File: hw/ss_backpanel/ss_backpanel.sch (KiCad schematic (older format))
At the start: 8 parts

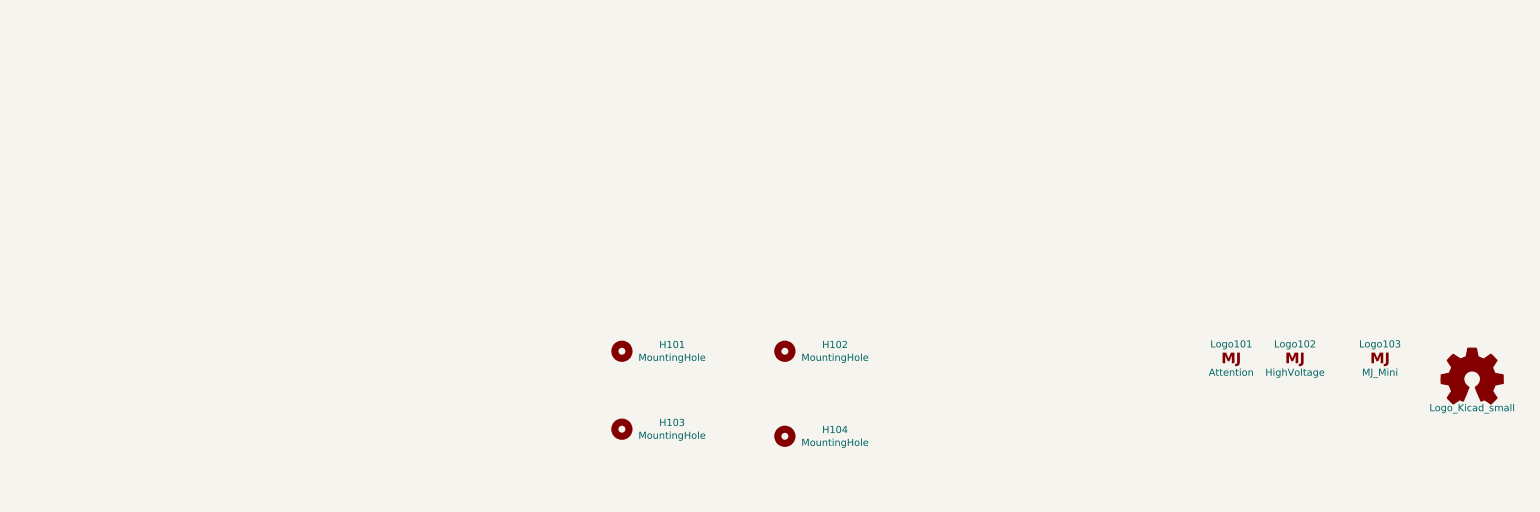
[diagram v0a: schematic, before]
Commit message: Backpanel: Initial placement of Schaffner AC-inlet, Schurter secondary fuse-holder and 2x Weller DIN7
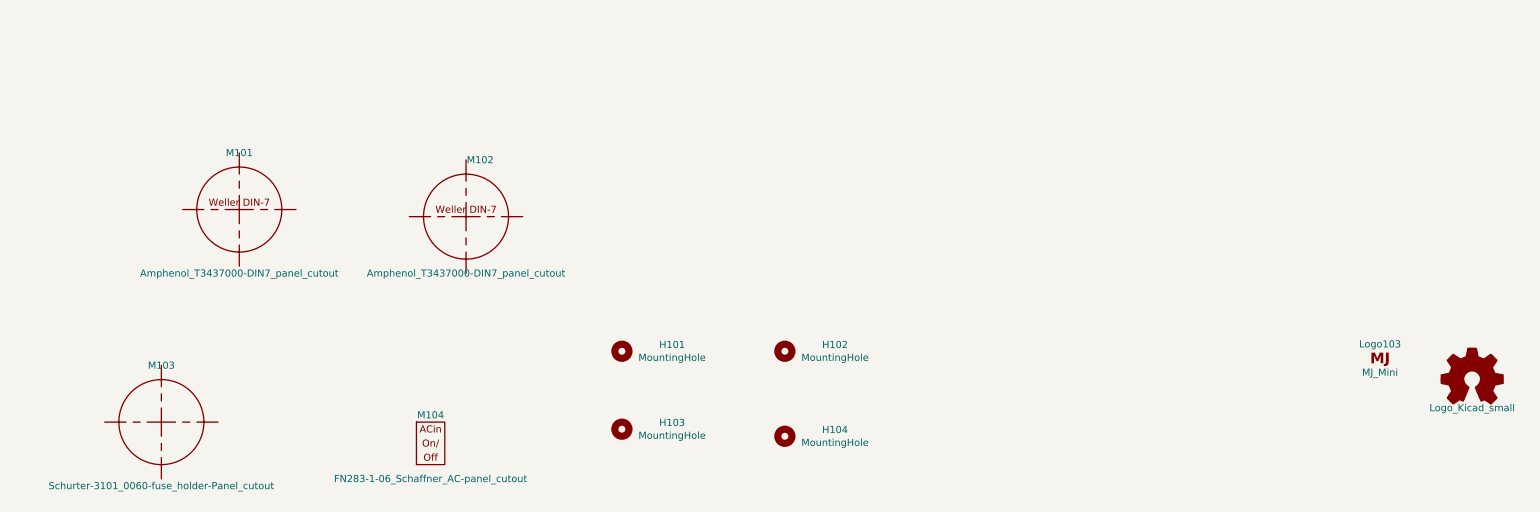
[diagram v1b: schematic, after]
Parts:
- removed Logo101: Attention, Symbol:Symbol_Attention_CopperTop_Big, symbol customlib_mj:Logo_MJ
- removed Logo102: HighVoltage, Symbol:Symbol_HighVoltage_Type2_CopperTop_Big, symbol customlib_mj:Logo_MJ
- added M101, M102: Amphenol_T3437000-DIN7_panel_cutout, customlib_mj_fp:Amphenol_T3437000-DIN7-panel_cutout, symbol customlib_mj:Amphenol_T3437000-DIN7_panel_cutout
- added M103: Schurter-3101_0060-fuse_holder-Panel_cutout, customlib_mj_fp:Schurter_3101_0060_fuse_holder-panel_cutout, symbol customlib_mj:Schurter-3101_0060-fuse_holder-Panel_cutout
- added M104: FN283-1-06_Schaffner_AC-panel_cutout, customlib_mj_fp:FN283_panel_cutout-outside_mnt, symbol customlib_mj:FN283-1-06_Schaffner_AC-panel_cutout
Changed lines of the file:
@@
-$EndComp
-$Comp
-L customlib_mj:Logo_MJ Logo102
-U 1 1 5F41EB17
-P 9500 6750
-F 0 "Logo102" H 9500 6850 50  0000 C CNN
-F 1 "HighVoltage" H 9500 6650 50  0000 C CNN
-F 2 "Symbol:Symbol_HighVoltage_Type2_CopperTop_Big" H 9500 6750 50  0001 C CNN
-F 3 "" H 9500 6750 50  0001 C CNN
-	1    9500 6750
-	1    0    0    -1
 $EndComp
 $Comp
@@
 $EndComp
 $Comp
-L customlib_mj:Logo_MJ Logo101
-U 1 1 5F41FBAB
-P 9050 6750
-F 0 "Logo101" H 9050 6850 50  0000 C CNN
-F 1 "Attention" H 9050 6650 50  0000 C CNN
-F 2 "Symbol:Symbol_Attention_CopperTop_Big" H 9050 6750 50  0001 C CNN
-F 3 "" H 9050 6750 50  0001 C CNN
-	1    9050 6750
+L customlib_mj:FN283-1-06_Schaffner_AC-panel_cutout M104
+U 1 1 5F4FFAD8
+P 3400 7350
+F 0 "M104" H 3400 7550 50  0000 C CNN
+F 1 "FN283-1-06_Schaffner_AC-panel_cutout" H 3400 7100 50  0000 C CNN
+F 2 "customlib_mj_fp:FN283_panel_cutout-outside_mnt" H 3400 7350 50  0001 C CNN
+F 3 "" H 3400 7350 50  0001 C CNN
+	1    3400 7350
 	1    0    0    -1
 $EndComp
+$Comp
+L customlib_mj:Schurter-3101_0060-fuse_holder-Panel_cutout M103
+U 1 1 5F50285E
+P 1500 7200
+F 0 "M103" H 1500 7600 50  0000 C CNN
+F 1 "Schurter-3101_0060-fuse_holder-Panel_cutout" H 1500 6750 50  0000 C CNN
+F 2 "customlib_mj_fp:Schurter_3101_0060_fuse_holder-panel_cutout" H 1500 7200 50  0001 C CNN
+F 3 "" H 1500 7200 50  0001 C CNN
+	1    1500 7200
+	1    0    0    -1
+$EndComp
+$Comp
+L customlib_mj:Amphenol_T3437000-DIN7_panel_cutout M101
+U 1 1 5F50426A
+P 2050 5700
+F 0 "M101" H 2050 6100 50  0000 C CNN
+F 1 "Amphenol_T3437000-DIN7_panel_cutout" H 2050 5250 50  0000 C CNN
+F 2 "customlib_mj_fp:Amphenol_T3437000-DIN7-panel_cutout" H 2050 5700 50  0001 C CNN
+F 3 "" H 2050 5700 50  0001 C CNN
+	1    2050 5700
+	1    0    0    -1
+$EndComp
+$Comp
+L customlib_mj:Amphenol_T3437000-DIN7_panel_cutout M102
+U 1 1 5F504C41
+P 3650 5750
+F 0 "M102" H 3750 6150 50  0000 C CNN
+F 1 "Amphenol_T3437000-DIN7_panel_cutout" H 3650 5350 50  0000 C CNN
+F 2 "customlib_mj_fp:Amphenol_T3437000-DIN7-panel_cutout" H 3650 5750 50  0001 C CNN
+F 3 "" H 3650 5750 50  0001 C CNN
+	1    3650 5750
+	1    0    0    -1
+$EndComp

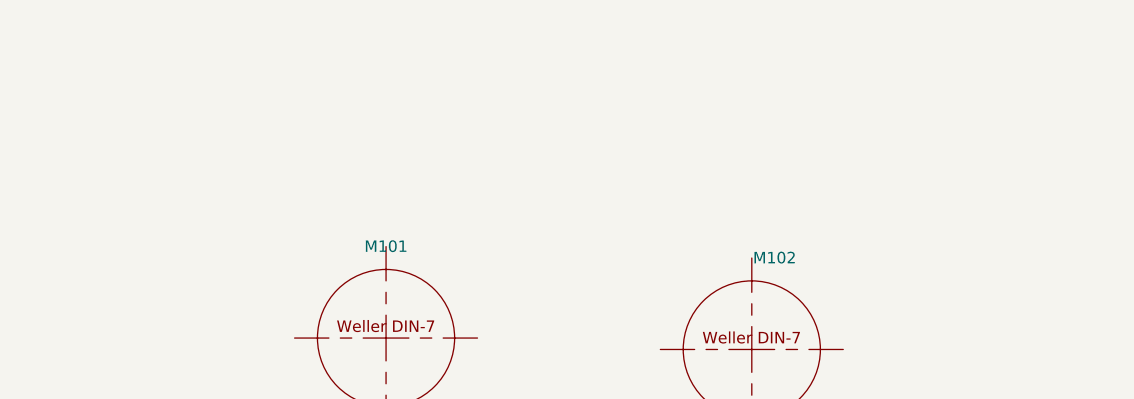
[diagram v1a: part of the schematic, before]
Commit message: Added back-panel cutouts for Wurth RJ45 (LAN) and TE's USB-A & USB-B connectors
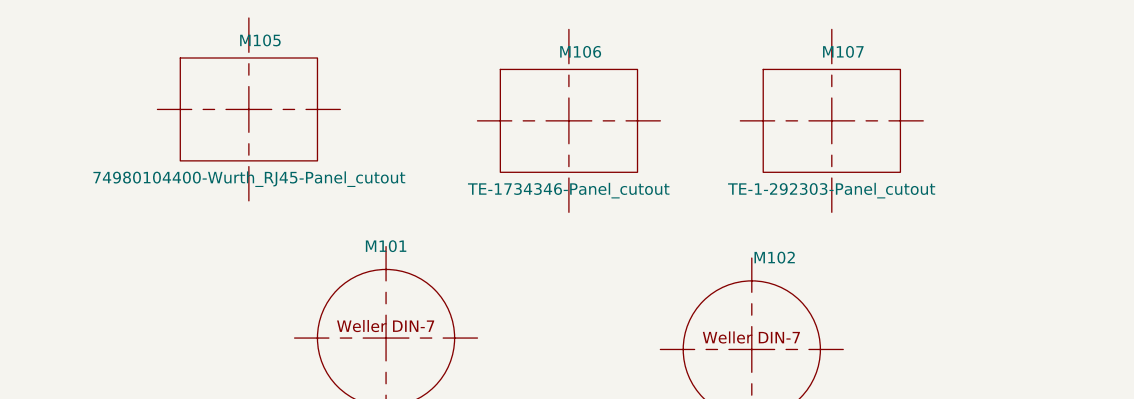
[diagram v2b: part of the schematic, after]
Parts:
- added M105: 74980104400-Wurth_RJ45-Panel_cutout, customlib_mj_fp:74980104400_WE_RJ45_LAN-Panel_cutout, symbol customlib_mj:74980104400-Wurth_RJ45-Panel_cutout
- added M106: TE-1734346-Panel_cutout, customlib_mj_fp:TE_1734346-Panel_cutout, symbol customlib_mj:TE-1734346-Panel_cutout
- added M107: TE-1-292303-Panel_cutout, customlib_mj_fp:TE_1-292303-Panel_cutout, symbol customlib_mj:TE-1-292303-Panel_cutout
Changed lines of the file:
@@
+	1    0    0    -1
+$EndComp
+$Comp
+L customlib_mj:74980104400-Wurth_RJ45-Panel_cutout M105
+U 1 1 5F4D2201
+P 1450 4700
+F 0 "M105" H 1500 5000 50  0000 C CNN
+F 1 "74980104400-Wurth_RJ45-Panel_cutout" H 1450 4400 50  0000 C CNN
+F 2 "customlib_mj_fp:74980104400_WE_RJ45_LAN-Panel_cutout" H 1450 4700 50  0001 C CNN
+F 3 "" H 1450 4700 50  0001 C CNN
+	1    1450 4700
+	1    0    0    -1
+$EndComp
+$Comp
+L customlib_mj:TE-1734346-Panel_cutout M106
+U 1 1 5F4D36E9
+P 2850 4750
+F 0 "M106" H 2900 5050 50  0000 C CNN
+F 1 "TE-1734346-Panel_cutout" H 2850 4450 50  0000 C CNN
+F 2 "customlib_mj_fp:TE_1734346-Panel_cutout" H 2850 4750 50  0001 C CNN
+F 3 "" H 2850 4750 50  0001 C CNN
+	1    2850 4750
+	1    0    0    -1
+$EndComp
+$Comp
+L customlib_mj:TE-1-292303-Panel_cutout M107
+U 1 1 5F4D4611
+P 4000 4750
+F 0 "M107" H 4050 5050 50  0000 C CNN
+F 1 "TE-1-292303-Panel_cutout" H 4000 4450 50  0000 C CNN
+F 2 "customlib_mj_fp:TE_1-292303-Panel_cutout" H 4000 4750 50  0001 C CNN
+F 3 "" H 4000 4750 50  0001 C CNN
+	1    4000 4750
 	1    0    0    -1
 $EndComp

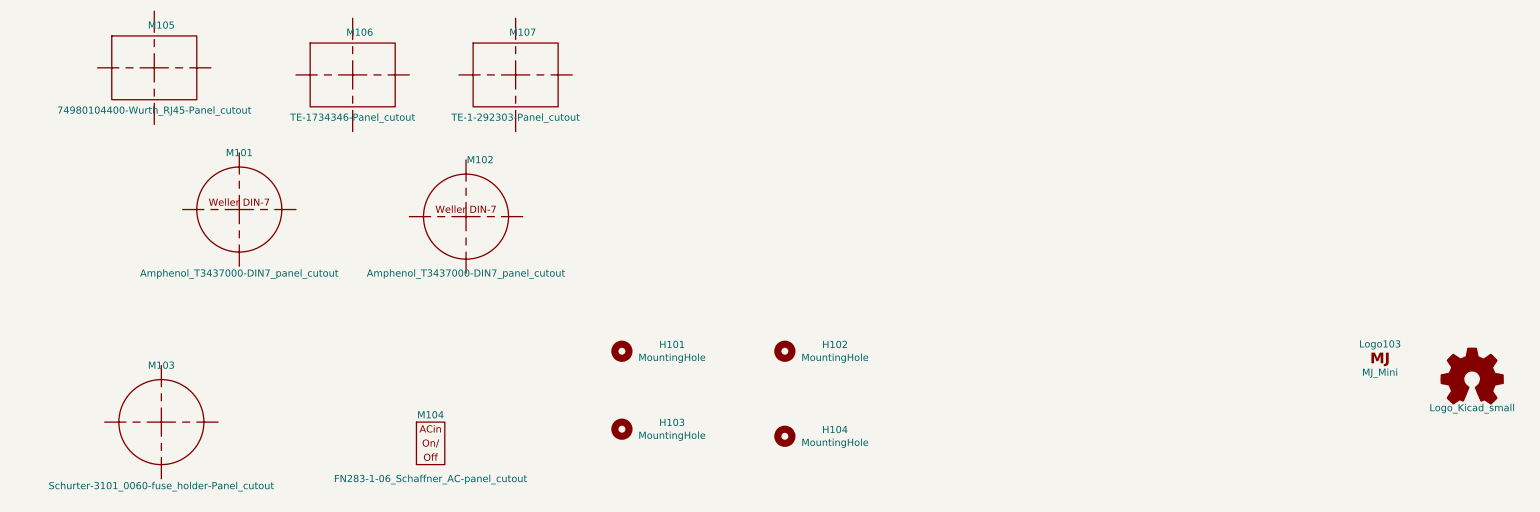
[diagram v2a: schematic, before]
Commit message: Updated back-panel with 3.5mm audio jack & Dsub-9 cut-outs
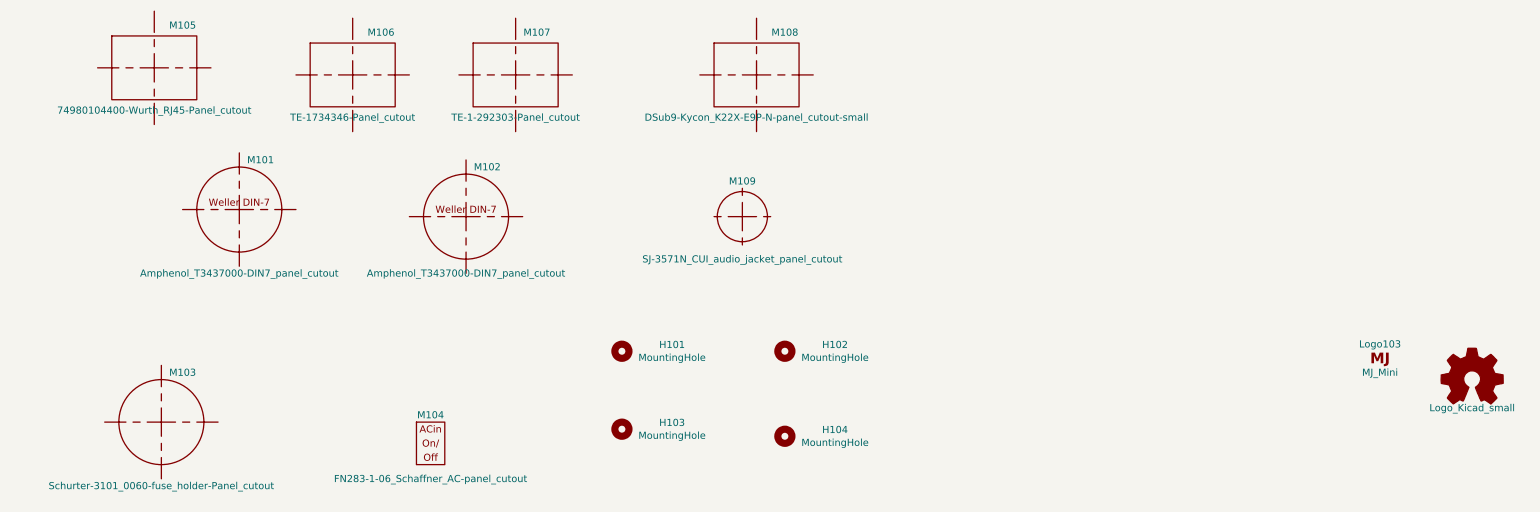
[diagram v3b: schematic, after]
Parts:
- added M108: DSub9-Kycon_K22X-E9P-N-panel_cutout-small, customlib_mj_fp:DSub9-Kycon_K22X-E9P-N_panel_cutout_behind, symbol customlib_mj:DSub9-Kycon_K22X-E9P-N-panel_cutout-small
- added M109: SJ-3571N_CUI_audio_jacket_panel_cutout, customlib_mj_fp:SJ-3571N_panel_cutout, symbol customlib_mj:SJ-3571N_CUI_audio_jacket_panel_cutout
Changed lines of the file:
@@
 U 1 1 5F50285E
 P 1500 7200
-F 0 "M103" H 1500 7600 50  0000 C CNN
+F 0 "M103" H 1650 7550 50  0000 C CNN
 F 1 "Schurter-3101_0060-fuse_holder-Panel_cutout" H 1500 6750 50  0000 C CNN
 F 2 "customlib_mj_fp:Schurter_3101_0060_fuse_holder-panel_cutout" H 1500 7200 50  0001 C CNN
@@
 U 1 1 5F50426A
 P 2050 5700
-F 0 "M101" H 2050 6100 50  0000 C CNN
+F 0 "M101" H 2200 6050 50  0000 C CNN
 F 1 "Amphenol_T3437000-DIN7_panel_cutout" H 2050 5250 50  0000 C CNN
 F 2 "customlib_mj_fp:Amphenol_T3437000-DIN7-panel_cutout" H 2050 5700 50  0001 C CNN
@@
 U 1 1 5F504C41
 P 3650 5750
-F 0 "M102" H 3750 6150 50  0000 C CNN
+F 0 "M102" H 3800 6100 50  0000 C CNN
 F 1 "Amphenol_T3437000-DIN7_panel_cutout" H 3650 5350 50  0000 C CNN
 F 2 "customlib_mj_fp:Amphenol_T3437000-DIN7-panel_cutout" H 3650 5750 50  0001 C CNN
@@
 U 1 1 5F4D2201
 P 1450 4700
-F 0 "M105" H 1500 5000 50  0000 C CNN
+F 0 "M105" H 1650 5000 50  0000 C CNN
 F 1 "74980104400-Wurth_RJ45-Panel_cutout" H 1450 4400 50  0000 C CNN
 F 2 "customlib_mj_fp:74980104400_WE_RJ45_LAN-Panel_cutout" H 1450 4700 50  0001 C CNN
@@
 U 1 1 5F4D36E9
 P 2850 4750
-F 0 "M106" H 2900 5050 50  0000 C CNN
+F 0 "M106" H 3050 5050 50  0000 C CNN
 F 1 "TE-1734346-Panel_cutout" H 2850 4450 50  0000 C CNN
 F 2 "customlib_mj_fp:TE_1734346-Panel_cutout" H 2850 4750 50  0001 C CNN
@@
 U 1 1 5F4D4611
 P 4000 4750
-F 0 "M107" H 4050 5050 50  0000 C CNN
+F 0 "M107" H 4150 5050 50  0000 C CNN
 F 1 "TE-1-292303-Panel_cutout" H 4000 4450 50  0000 C CNN
 F 2 "customlib_mj_fp:TE_1-292303-Panel_cutout" H 4000 4750 50  0001 C CNN
@@
 	1    0    0    -1
 $EndComp
+$Comp
+L customlib_mj:DSub9-Kycon_K22X-E9P-N-panel_cutout-small M108
+U 1 1 5F4DCFFF
+P 5700 4750
+F 0 "M108" H 5900 5050 50  0000 C CNN
+F 1 "DSub9-Kycon_K22X-E9P-N-panel_cutout-small" H 5700 4450 50  0000 C CNN
+F 2 "customlib_mj_fp:DSub9-Kycon_K22X-E9P-N_panel_cutout_behind" H 5700 4750 50  0001 C CNN
+F 3 "" H 5700 4750 50  0001 C CNN
+	1    5700 4750
+	1    0    0    -1
+$EndComp
+$Comp
+L customlib_mj:SJ-3571N_CUI_audio_jacket_panel_cutout M109
+U 1 1 5F4E1D6C
+P 5600 5750
+F 0 "M109" H 5600 6000 50  0000 C CNN
+F 1 "SJ-3571N_CUI_audio_jacket_panel_cutout" H 5600 5450 50  0000 C CNN
+F 2 "customlib_mj_fp:SJ-3571N_panel_cutout" H 5600 5750 50  0001 C CNN
+F 3 "" H 5600 5750 50  0001 C CNN
+	1    5600 5750
+	1    0    0    -1
+$EndComp

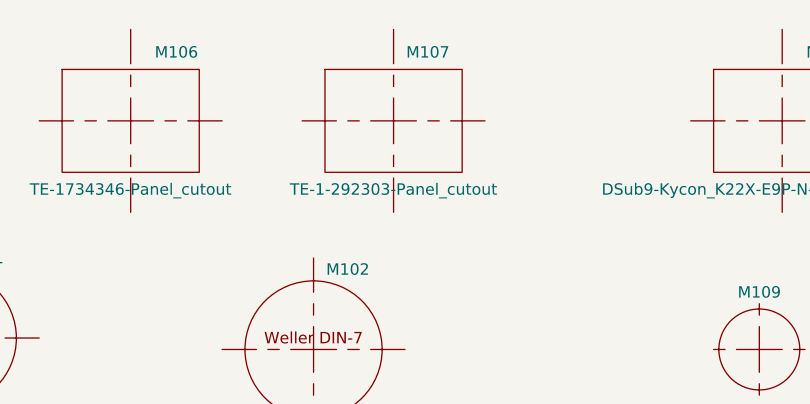
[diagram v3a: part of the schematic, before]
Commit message: Updated USB-A conn to CUI UJ2-AH-1-SMT because retention pads are SMD. Also better USB-A cutout in back panel. Updated 3d test model
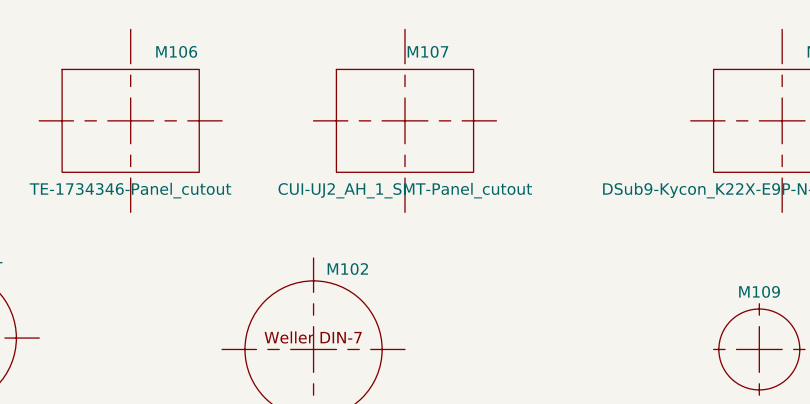
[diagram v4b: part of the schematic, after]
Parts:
- removed M107: TE-1-292303-Panel_cutout, customlib_mj_fp:TE_1-292303-Panel_cutout, symbol customlib_mj:TE-1-292303-Panel_cutout
- added M107: CUI-UJ2_AH_1_SMT-Panel_cutout, customlib_mj_fp:CUI-UJ2_AH_1_SMT-Panel_cutout, symbol customlib_mj:CUI-UJ2_AH_1_SMT-Panel_cutout
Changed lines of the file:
@@
-$EndComp
-$Comp
-L customlib_mj:TE-1-292303-Panel_cutout M107
-U 1 1 5F4D4611
-P 4000 4750
-F 0 "M107" H 4150 5050 50  0000 C CNN
-F 1 "TE-1-292303-Panel_cutout" H 4000 4450 50  0000 C CNN
-F 2 "customlib_mj_fp:TE_1-292303-Panel_cutout" H 4000 4750 50  0001 C CNN
-F 3 "" H 4000 4750 50  0001 C CNN
-	1    4000 4750
-	1    0    0    -1
 $EndComp
 $Comp
@@
 	1    0    0    -1
 $EndComp
+$Comp
+L customlib_mj:CUI-UJ2_AH_1_SMT-Panel_cutout M107
+U 1 1 5F7D0AEA
+P 4050 4750
+F 0 "M107" H 4150 5050 50  0000 C CNN
+F 1 "CUI-UJ2_AH_1_SMT-Panel_cutout" H 4050 4450 50  0000 C CNN
+F 2 "customlib_mj_fp:CUI-UJ2_AH_1_SMT-Panel_cutout" H 4050 4750 50  0001 C CNN
+F 3 "" H 4050 4750 50  0001 C CNN
+	1    4050 4750
+	1    0    0    -1
+$EndComp

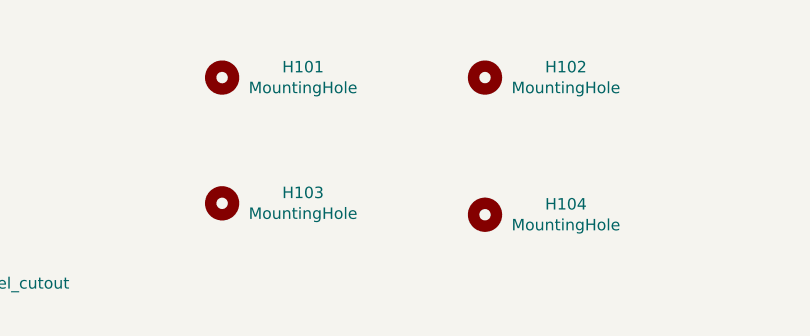
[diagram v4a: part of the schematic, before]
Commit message: Added 4mm banana earth connector to back panel. Moved DIN-connectors slightly to fit. Updated 3d test model
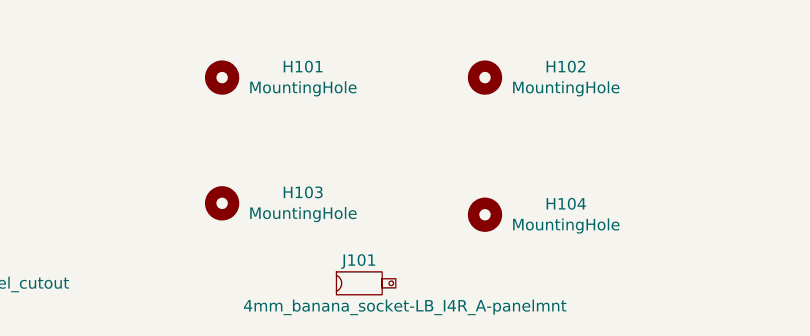
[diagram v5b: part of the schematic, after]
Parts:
- added J101: 4mm_banana_socket-LB_I4R_A-panelmnt, customlib_mj_fp:LB_I4R_A-4mm_banana_socket_panelmnt, symbol customlib_mj:4mm_banana_socket-LB_I4R_A-panelmnt
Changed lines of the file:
@@
+	1    0    0    -1
+$EndComp
+$Comp
+L customlib_mj:4mm_banana_socket-LB_I4R_A-panelmnt J101
+U 1 1 5F7FEDE6
+P 5300 7600
+F 0 "J101" H 5350 7700 50  0000 C CNN
+F 1 "4mm_banana_socket-LB_I4R_A-panelmnt" H 5550 7500 50  0000 C CNN
+F 2 "customlib_mj_fp:LB_I4R_A-4mm_banana_socket_panelmnt" H 5300 7600 50  0001 C CNN
+F 3 "https://www.elfa.se/Web/Downloads/_t/ds/LB-I4R-A_B_eng_fre_ger_tds.pdf" H 5300 7600 50  0001 C CNN
+	1    5300 7600
 	1    0    0    -1
 $EndComp
